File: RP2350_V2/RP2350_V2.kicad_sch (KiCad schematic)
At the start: 114 parts, among them IC1 DMP1045U-7, IC2 DMP1045U-7, IC3 DMP1045U-7, IC4 DMP1045U-7, IC5 DMP1045U-7, IC6 DMP1045U-7, J1 Conn_01x04_Pin, J10 S0991-46R, J2 S0991-46R, J3 USB_C_Receptacle_USB2.0_16P, J5 Conn_01x08_Socket, J6 Conn_01x02_Pin, J7 Conn_01x04_Pin, J8 S0991-46R, J9 S0991-46R, SW1 PTS 647 SN50 SMTR2 LFS, SW10 PTS 647 SN50 SMTR2 LFS, SW11 PTS 647 SN50 SMTR2 LFS, SW12 PTS 647 SN50 SMTR2 LFS, SW13 PTS 647 SN50 SMTR2 LFS, SW14 PTS 647 SN50 SMTR2 LFS, SW4 PTS 647 SN50 SMTR2 LFS, SW9 PTS 647 SN50 SMTR2 LFS, U1 RP2350_60QFN, U2 W25Q128JVS, U3 TPS62811QWRWYRQ1, U4 MCP73812T-420I-OT, U5 TLV3012AIDCKR, U6 74HC14, X1 ABM8-272-T3

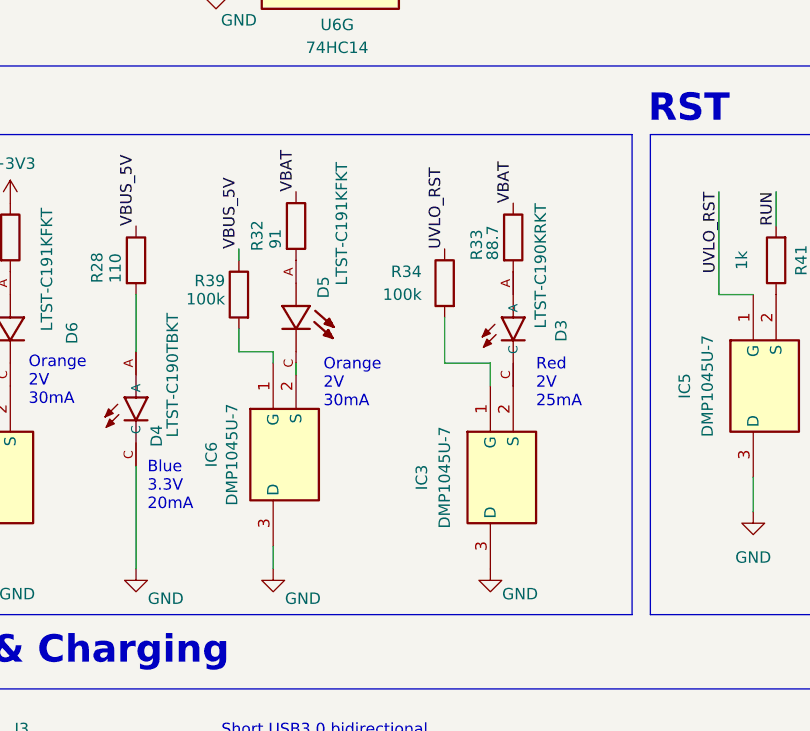
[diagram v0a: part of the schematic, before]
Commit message: fixed RF impedance matched width, changed rf connector, etc.
DRC+DFM clean with waivers. Pending final review for tapeout.
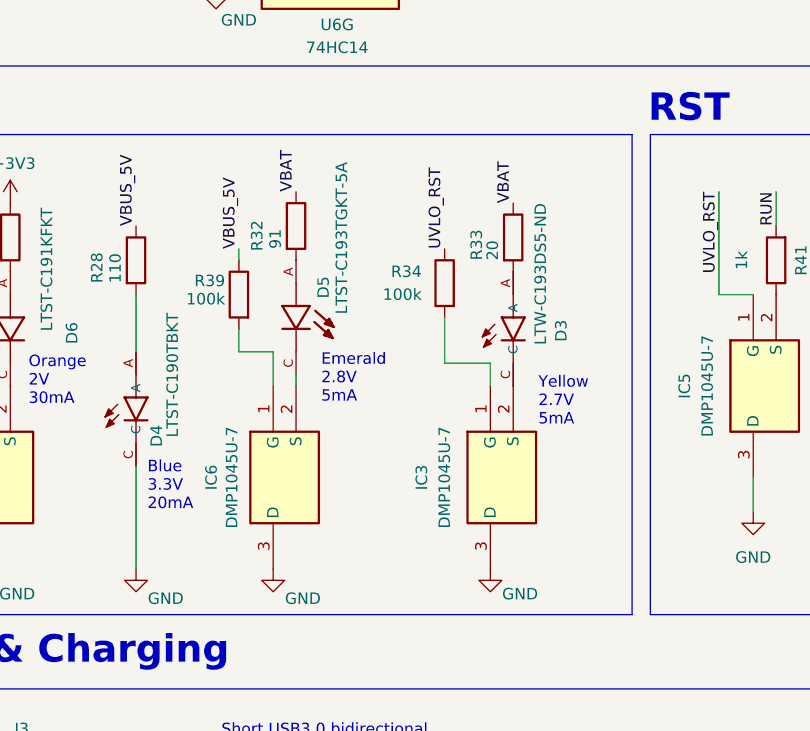
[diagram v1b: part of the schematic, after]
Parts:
- D3: value LTST-C190KRKT -> LTW-C193DS5-ND
- D5: value LTST-C191KFKT -> LTST-C193TGKT-5A
- R33: value 88.7 -> 20; LCSC C423126 -> C25089
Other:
- note added: "Emerald 2.8V 5mA"
- note added: "Yellow 2.7V 5mA"
- note removed: "Red 2V 25mA"
- moved on the sheet: IC6

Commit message: tapeout files included, updated D3, D5 LCSC values (change reflected in order)
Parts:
- D3: LCSC C94869 -> C161619
- D5: LCSC C160478 -> C12065
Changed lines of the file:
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@@
 			)
 		)
-		(property "LCSC" "C94869"
+		(property "LCSC" "C161619"
 			(at 90.17 172.72 0)
 			(effects
@@
 			)
 		)
-		(property "LCSC" "C160478"
+		(property "LCSC" "C12065"
 			(at 66.04 171.45 0)
 			(effects
